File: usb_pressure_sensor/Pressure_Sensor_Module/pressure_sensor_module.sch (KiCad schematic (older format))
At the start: 3 parts, among them IC1 MS580314BA01-00, J1 MODULE_BRIDGE

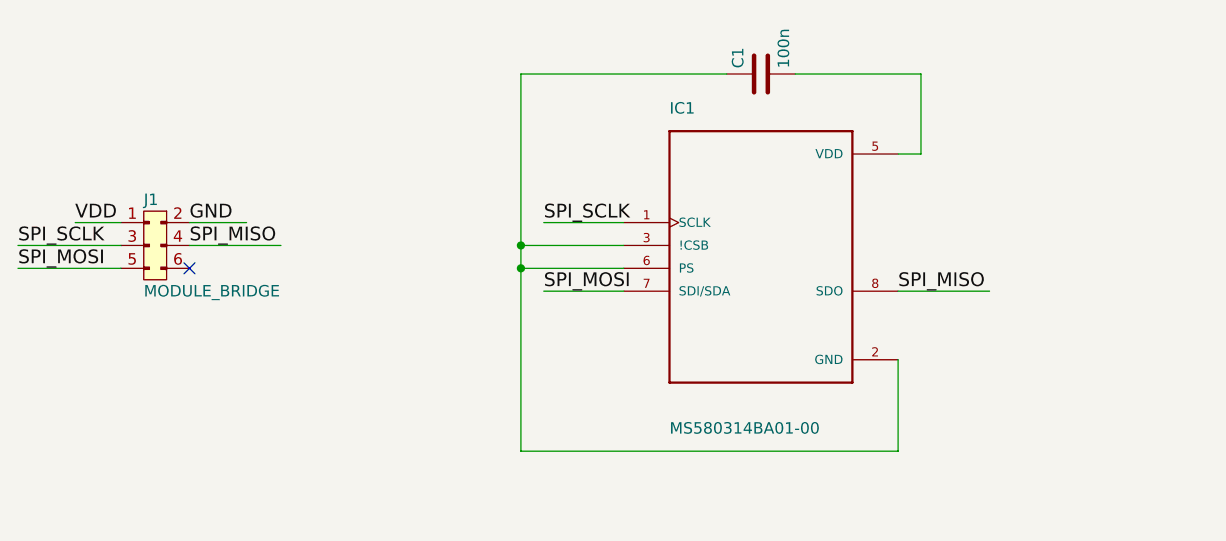
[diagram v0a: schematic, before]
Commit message: Added PCB for pressure module
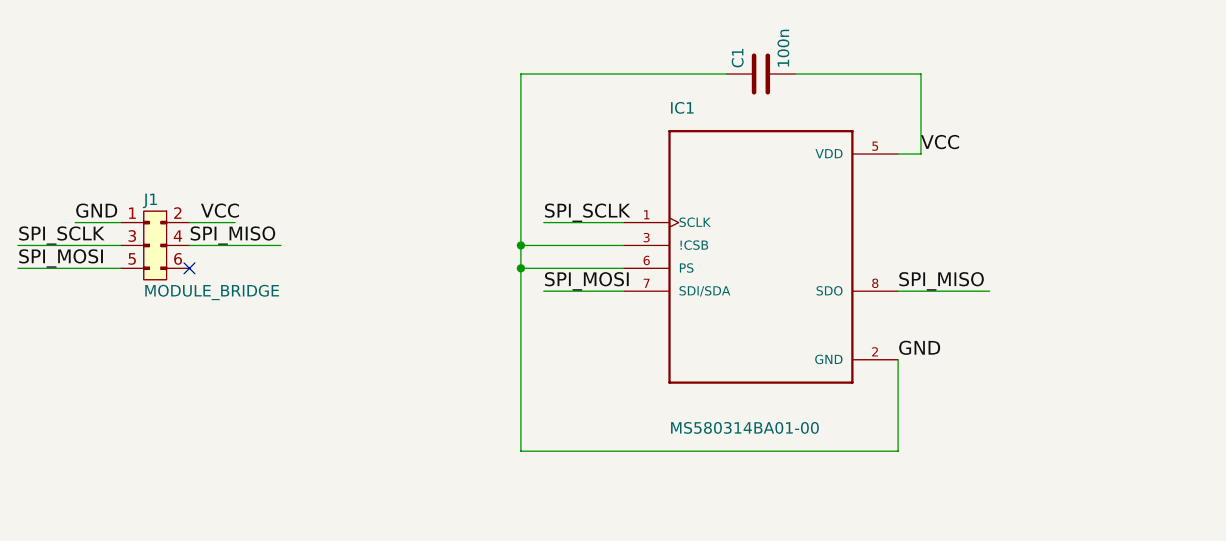
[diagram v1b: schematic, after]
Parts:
- C1: footprint (none) -> Capacitors_SMD:C_0603
- IC1: footprint XDCR_MS580314BA01-00 -> footprints:XDCR_MS580314BA01-00
- J1: footprint (none) -> Socket_Strips:Socket_Strip_Straight_2x03_Pitch2.54mm
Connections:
- net labels added: VCC
- net labels removed: VDD
- wire segments 19 -> 17
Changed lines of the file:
@@
 LIBS:cauv_lib
 LIBS:agg-kicad
+LIBS:pressure_sensor_module-cache
 EELAYER 25 0
 EELAYER END
@@
 F 0 "IC1" H 5300 3900 50  0000 L CNN
 F 1 "MS580314BA01-00" H 5300 2500 50  0000 L CNN
-F 2 "XDCR_MS580314BA01-00" H 6050 2600 50  0001 L CNN
+F 2 "footprints:XDCR_MS580314BA01-00" H 6050 2600 50  0001 L CNN
 F 3 "17.19 USD" H 5850 3950 50  0001 L CNN
 	1    5700 3300
 	1    0    0    -1
 $EndComp
-Wire Wire Line
-	6300 2900 6400 2900
-Wire Wire Line
-	6400 2900 6400 2550
 $Comp
 L C C1
@@
 F 0 "C1" H 5725 2650 50  0000 L CNN
 F 1 "100n" H 5725 2450 50  0000 L CNN
-F 2 "" H 5738 2400 50  0001 C CNN
+F 2 "Capacitors_SMD:C_0603" H 5738 2400 50  0001 C CNN
 F 3 "" H 5700 2550 50  0001 C CNN
 	1    5700 2550
 	0    -1   -1   0
 $EndComp
+Text Label 4750 3200 0    60   ~ 0
+SPI_SCLK
+Text Label 4750 3500 0    60   ~ 0
+SPI_MOSI
+Text Label 6300 3500 0    60   ~ 0
+SPI_MISO
+$Comp
+L CONN_02x03 J1
+U 1 1 59948937
+P 3100 3200
+F 0 "J1" H 3000 3300 50  0000 L CNN
+F 1 "MODULE_BRIDGE" H 3000 2900 50  0000 L CNN
+F 2 "Socket_Strips:Socket_Strip_Straight_2x03_Pitch2.54mm" H 3100 3200 50  0001 C CNN
+F 3 "" H 3100 3200 50  0001 C CNN
+	1    3100 3200
+	1    0    0    -1
+$EndComp
+Text Label 2450 3300 0    60   ~ 0
+SPI_SCLK
+Text Label 2450 3400 0    60   ~ 0
+SPI_MOSI
+Text Label 3200 3300 0    60   ~ 0
+SPI_MISO
+NoConn ~ 3200 3400
+Text Label 2700 3200 0    60   ~ 0
+GND
+Text Label 3250 3200 0    60   ~ 0
+VCC
+Text Label 6300 3800 0    60   ~ 0
+GND
+Text Label 6400 2900 0    60   ~ 0
+VCC
+Wire Wire Line
+	6300 2900 6400 2900
+Wire Wire Line
+	6400 2900 6400 2550
 Wire Wire Line
 	6400 2550 5850 2550
@@
 Wire Wire Line
 	5100 3500 4750 3500
-Text Label 4750 3200 0    60   ~ 0
-SPI_SCLK
-Text Label 4750 3500 0    60   ~ 0
-SPI_MOSI
 Wire Wire Line
 	5550 2550 4650 2550
 Wire Wire Line
-	4650 2550 4650 3300
-Wire Wire Line
-	4650 3300 4650 3400
-Wire Wire Line
-	4650 3400 4650 4200
+	4650 2550 4650 4200
 Wire Wire Line
 	5100 3400 4650 3400
@@
 Wire Wire Line
 	6300 3500 6700 3500
-Text Label 6300 3500 0    60   ~ 0
-SPI_MISO
-$Comp
-L CONN_02x03 J1
-U 1 1 59948937
-P 3100 3200
-F 0 "J1" H 3000 3300 50  0000 L CNN
-F 1 "MODULE_BRIDGE" H 3000 2900 50  0000 L CNN
-F 2 "" H 3100 3200 50  0001 C CNN
-F 3 "" H 3100 3200 50  0001 C CNN
-	1    3100 3200
-	1    0    0    -1
-$EndComp
 Wire Wire Line
 	2450 3300 2900 3300
@@
 	3200 3300 3600 3300
 Wire Wire Line
-	3200 3200 3450 3200
-Text Label 2700 3200 0    60   ~ 0
-VDD
+	3200 3200 3400 3200
 Wire Wire Line
 	2900 3200 2700 3200
-Text Label 3200 3200 0    60   ~ 0
-GND
-Text Label 2450 3300 0    60   ~ 0
-SPI_SCLK
-Text Label 2450 3400 0    60   ~ 0
-SPI_MOSI
-Text Label 3200 3300 0    60   ~ 0
-SPI_MISO
-NoConn ~ 3200 3400
 $EndSCHEMATC

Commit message: First iteration with new pressure sensor
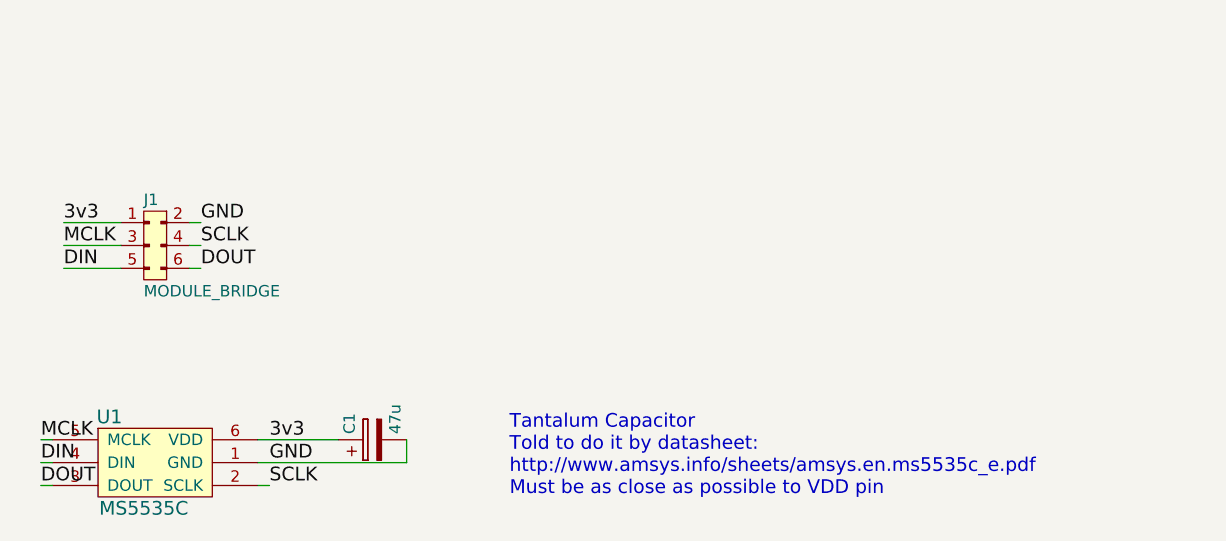
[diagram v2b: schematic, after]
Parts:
- removed C1: 100n, Capacitors_SMD:C_0603, symbol C
- removed IC1: MS580314BA01-00, footprints:XDCR_MS580314BA01-00, symbol MS580314BA01-00
- added C1: 47u, symbol CP
- added U1: MS5535C, symbol MS5535C
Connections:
- net labels added: 3v3, DIN, DOUT, MCLK, SCLK
- net labels removed: SPI_MISO, SPI_MOSI, SPI_SCLK, VCC
- wire segments 17 -> 13
- no-connect marks 1 -> 0
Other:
- note added: "Tantalum Capacitor\nTold to do it by datasheet: \nhttp://www.amsys.info/sheets/amsys.en.ms5535c_e.pdf\nMust be as close as possible to VDD pin"
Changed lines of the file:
@@
 $EndDescr
-$Comp
-L MS580314BA01-00 IC1
-U 1 1 59948538
-P 5700 3300
-F 0 "IC1" H 5300 3900 50  0000 L CNN
-F 1 "MS580314BA01-00" H 5300 2500 50  0000 L CNN
-F 2 "footprints:XDCR_MS580314BA01-00" H 6050 2600 50  0001 L CNN
-F 3 "17.19 USD" H 5850 3950 50  0001 L CNN
-	1    5700 3300
-	1    0    0    -1
-$EndComp
-$Comp
-L C C1
-U 1 1 599485E2
-P 5700 2550
-F 0 "C1" H 5725 2650 50  0000 L CNN
-F 1 "100n" H 5725 2450 50  0000 L CNN
-F 2 "Capacitors_SMD:C_0603" H 5738 2400 50  0001 C CNN
-F 3 "" H 5700 2550 50  0001 C CNN
-	1    5700 2550
-	0    -1   -1   0
-$EndComp
-Text Label 4750 3200 0    60   ~ 0
-SPI_SCLK
-Text Label 4750 3500 0    60   ~ 0
-SPI_MOSI
-Text Label 6300 3500 0    60   ~ 0
-SPI_MISO
 $Comp
 L CONN_02x03 J1
@@
 	1    0    0    -1
 $EndComp
-Text Label 2450 3300 0    60   ~ 0
-SPI_SCLK
-Text Label 2450 3400 0    60   ~ 0
-SPI_MOSI
-Text Label 3200 3300 0    60   ~ 0
-SPI_MISO
-NoConn ~ 3200 3400
-Text Label 2700 3200 0    60   ~ 0
+Text Label 2650 3200 0    60   ~ 0
+3v3
+$Comp
+L MS5535C U1
+U 1 1 599945F8
+P 3050 4250
+F 0 "U1" H 2850 4450 60  0000 C CNN
+F 1 "MS5535C" H 3000 4050 60  0000 C CNN
+F 2 "" H 3100 4150 60  0001 C CNN
+F 3 "" H 3100 4150 60  0001 C CNN
+	1    3050 4250
+	1    0    0    -1
+$EndComp
+Text Label 2650 3300 0    60   ~ 0
+MCLK
+Text Label 2650 3400 0    60   ~ 0
+DIN
+Text Label 3250 3200 0    60   ~ 0
 GND
-Text Label 3250 3200 0    60   ~ 0
-VCC
-Text Label 6300 3800 0    60   ~ 0
+Text Label 3250 3300 0    60   ~ 0
+SCLK
+Text Label 3250 3400 0    60   ~ 0
+DOUT
+Text Label 2550 4150 0    60   ~ 0
+MCLK
+Text Label 2550 4250 0    60   ~ 0
+DIN
+Text Label 2550 4350 0    60   ~ 0
+DOUT
+Text Label 3550 4150 0    60   ~ 0
+3v3
+Text Label 3550 4250 0    60   ~ 0
 GND
-Text Label 6400 2900 0    60   ~ 0
-VCC
+Text Label 3550 4350 0    60   ~ 0
+SCLK
+Text Notes 4600 4400 0    60   ~ 0
+Tantalum Capacitor\nTold to do it by datasheet: \nhttp://www.amsys.info/sheets/amsys.en.ms5535c_e.pdf\nMust be as close as possible to VDD pin
 Wire Wire Line
-	6300 2900 6400 2900
+	2900 3200 2650 3200
 Wire Wire Line
-	6400 2900 6400 2550
+	2900 3300 2650 3300
 Wire Wire Line
-	6400 2550 5850 2550
+	2900 3400 2650 3400
 Wire Wire Line
-	5100 3200 4750 3200
+	3200 3200 3250 3200
 Wire Wire Line
-	5100 3500 4750 3500
+	3200 3300 3250 3300
 Wire Wire Line
-	5550 2550 4650 2550
+	3200 3400 3250 3400
 Wire Wire Line
-	4650 2550 4650 4200
+	2600 4150 2550 4150
 Wire Wire Line
-	5100 3400 4650 3400
-Connection ~ 4650 3400
+	2600 4250 2550 4250
 Wire Wire Line
-	5100 3300 4650 3300
-Connection ~ 4650 3300
+	2600 4350 2550 4350
 Wire Wire Line
-	4650 4200 6300 4200
+	3500 4150 3850 4150
 Wire Wire Line
-	6300 4200 6300 3800
+	3500 4250 4150 4250
 Wire Wire Line
-	6300 3500 6700 3500
+	3500 4350 3550 4350
 Wire Wire Line
-	2450 3300 2900 3300
-Wire Wire Line
-	2450 3400 2900 3400
-Wire Wire Line
-	3200 3300 3600 3300
-Wire Wire Line
-	3200 3200 3400 3200
-Wire Wire Line
-	2900 3200 2700 3200
+	4150 4250 4150 4150
+$Comp
+L CP C1
+U 1 1 59996212
+P 4000 4150
+F 0 "C1" H 4025 4250 50  0000 L CNN
+F 1 "47u" H 4025 4050 50  0000 L CNN
+F 2 "" H 4038 4000 50  0001 C CNN
+F 3 "" H 4000 4150 50  0001 C CNN
+	1    4000 4150
+	0    -1   -1   0
+$EndComp
 $EndSCHEMATC

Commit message: PCB design with new pressure sensor and some footprints
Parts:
- C1: footprint (none) -> Capacitors_Tantalum_SMD:CP_Tantalum_Case-C_EIA-6032-28_Reflow
- U1: footprint (none) -> footprints:MS5535C
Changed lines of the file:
@@
 F 0 "U1" H 2850 4450 60  0000 C CNN
 F 1 "MS5535C" H 3000 4050 60  0000 C CNN
-F 2 "" H 3100 4150 60  0001 C CNN
+F 2 "footprints:MS5535C" H 3100 4150 60  0001 C CNN
 F 3 "" H 3100 4150 60  0001 C CNN
 	1    3050 4250
@@
 F 0 "C1" H 4025 4250 50  0000 L CNN
 F 1 "47u" H 4025 4050 50  0000 L CNN
-F 2 "" H 4038 4000 50  0001 C CNN
+F 2 "Capacitors_Tantalum_SMD:CP_Tantalum_Case-C_EIA-6032-28_Reflow" H 4038 4000 50  0001 C CNN
 F 3 "" H 4000 4150 50  0001 C CNN
 	1    4000 4150
